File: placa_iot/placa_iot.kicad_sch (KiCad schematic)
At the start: 0 parts

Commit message: Esquemáticos creados
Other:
- added sheet ALIMENTACIÓN (alimentacion.kicad_sch)
- added sheet BATTERY (battery.kicad_sch)
- added sheet MICROCONTROLADOR (microcontrolador.kicad_sch)
- added sheet RF (rf.kicad_sch)
- company: (none) -> ELE0226
- title: (none) -> Placa IoT
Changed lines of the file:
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@@
 	(generator "eeschema")
 	(generator_version "10.0")
-	(paper "A4")
+	(paper "A3")
+	(title_block
+		(title "Placa IoT")
+		(date "2026-05-19")
+		(rev "R0")
+		(company "ELE0226")
+		(comment 1 "Sofía González Carranza")
+	)
+	(sheet
+		(at 40.64 151.13)
+		(size 105.41 92.71)
+		(exclude_from_sim no)
+		(in_bom yes)
+		(on_board yes)
+		(dnp no)
+		(fields_autoplaced yes)
+		(stroke
+			(width 0.1524)
+			(type solid)
+		)
+		(fill
+			(color 0 0 0 0)
+		)
+		(property "Sheetname" "RF"
+			(at 40.64 150.4184 0)
+			(show_name no)
+			(do_not_autoplace no)
+			(effects
+				(font
+					(size 1.27 1.27)
+				)
+				(justify left bottom)
+			)
+		)
+		(property "Sheetfile" "rf.kicad_sch"
+			(at 40.64 244.4246 0)
+			(show_name no)
+			(do_not_autoplace no)
+			(effects
+				(font
+					(size 1.27 1.27)
+				)
+				(justify left top)
+			)
+		)
+		(instances
+			(project "placa_iot"
+				(path "/ca8a6ff9-ef79-4432-921e-b6a14ecba63b"
+					(page "4")
+				)
+			)
+		)
+	)
+	(sheet
+		(at 38.1 38.1)
+		(size 107.95 90.17)
+		(exclude_from_sim no)
+		(in_bom yes)
+		(on_board yes)
+		(dnp no)
+		(fields_autoplaced yes)
+		(stroke
+			(width 0.1524)
+			(type solid)
+		)
+		(fill
+			(color 0 0 0 0)
+		)
+		(property "Sheetname" "ALIMENTACIÓN"
+			(at 38.1 37.3884 0)
+			(show_name no)
+			(do_not_autoplace no)
+			(effects
+				(font
+					(size 1.27 1.27)
+				)
+				(justify left bottom)
+			)
+		)
+		(property "Sheetfile" "alimentacion.kicad_sch"
+			(at 38.1 128.8546 0)
+			(show_name no)
+			(do_not_autoplace no)
+			(effects
+				(font
+					(size 1.27 1.27)
+				)
+				(justify left top)
+			)
+		)
+		(instances
+			(project "placa_iot"
+				(path "/ca8a6ff9-ef79-4432-921e-b6a14ecba63b"
+					(page "2")
+				)
+			)
+		)
+	)
+	(sheet
+		(at 294.64 85.09)
+		(size 99.06 109.22)
+		(exclude_from_sim no)
+		(in_bom yes)
+		(on_board yes)
+		(dnp no)
+		(fields_autoplaced yes)
+		(stroke
+			(width 0.1524)
+			(type solid)
+		)
+		(fill
+			(color 0 0 0 0)
+		)
+		(property "Sheetname" "BATTERY"
+			(at 294.64 84.3784 0)
+			(show_name no)
+			(do_not_autoplace no)
+			(effects
+				(font
+					(size 1.27 1.27)
+				)
+				(justify left bottom)
+			)
+		)
+		(property "Sheetfile" "battery.kicad_sch"
+			(at 294.64 194.8946 0)
+			(show_name no)
+			(do_not_autoplace no)
+			(effects
+				(font
+					(size 1.27 1.27)
+				)
+				(justify left top)
+			)
+		)
+		(instances
+			(project "placa_iot"
+				(path "/ca8a6ff9-ef79-4432-921e-b6a14ecba63b"
+					(page "5")
+				)
+			)
+		)
+	)
+	(sheet
+		(at 170.18 38.1)
+		(size 105.41 205.74)
+		(exclude_from_sim no)
+		(in_bom yes)
+		(on_board yes)
+		(dnp no)
+		(fields_autoplaced yes)
+		(stroke
+			(width 0.1524)
+			(type solid)
+		)
+		(fill
+			(color 0 0 0 0)
+		)
+		(property "Sheetname" "MICROCONTROLADOR"
+			(at 170.18 37.3884 0)
+			(show_name no)
+			(do_not_autoplace no)
+			(effects
+				(font
+					(size 1.27 1.27)
+				)
+				(justify left bottom)
+			)
+		)
+		(property "Sheetfile" "microcontrolador.kicad_sch"
+			(at 170.18 244.4246 0)
+			(show_name no)
+			(do_not_autoplace no)
+			(effects
+				(font
+					(size 1.27 1.27)
+				)
+				(justify left top)
+			)
+		)
+		(instances
+			(project "placa_iot"
+				(path "/ca8a6ff9-ef79-4432-921e-b6a14ecba63b"
+					(page "3")
+				)
+			)
+		)
+	)
 	(sheet_instances
 		(path "/"

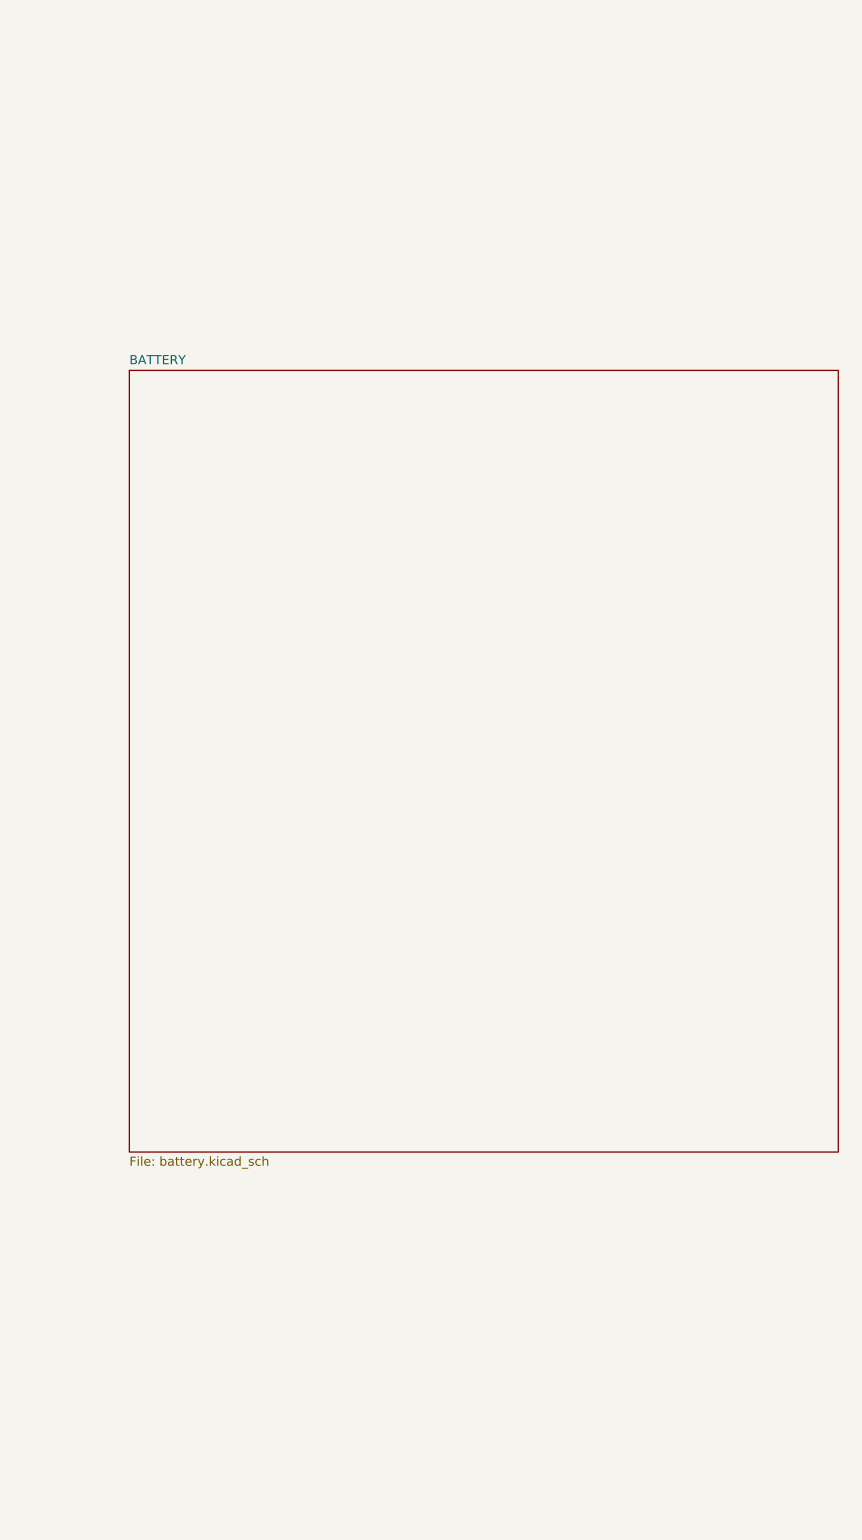
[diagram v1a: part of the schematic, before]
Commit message: Esquemático USB completado
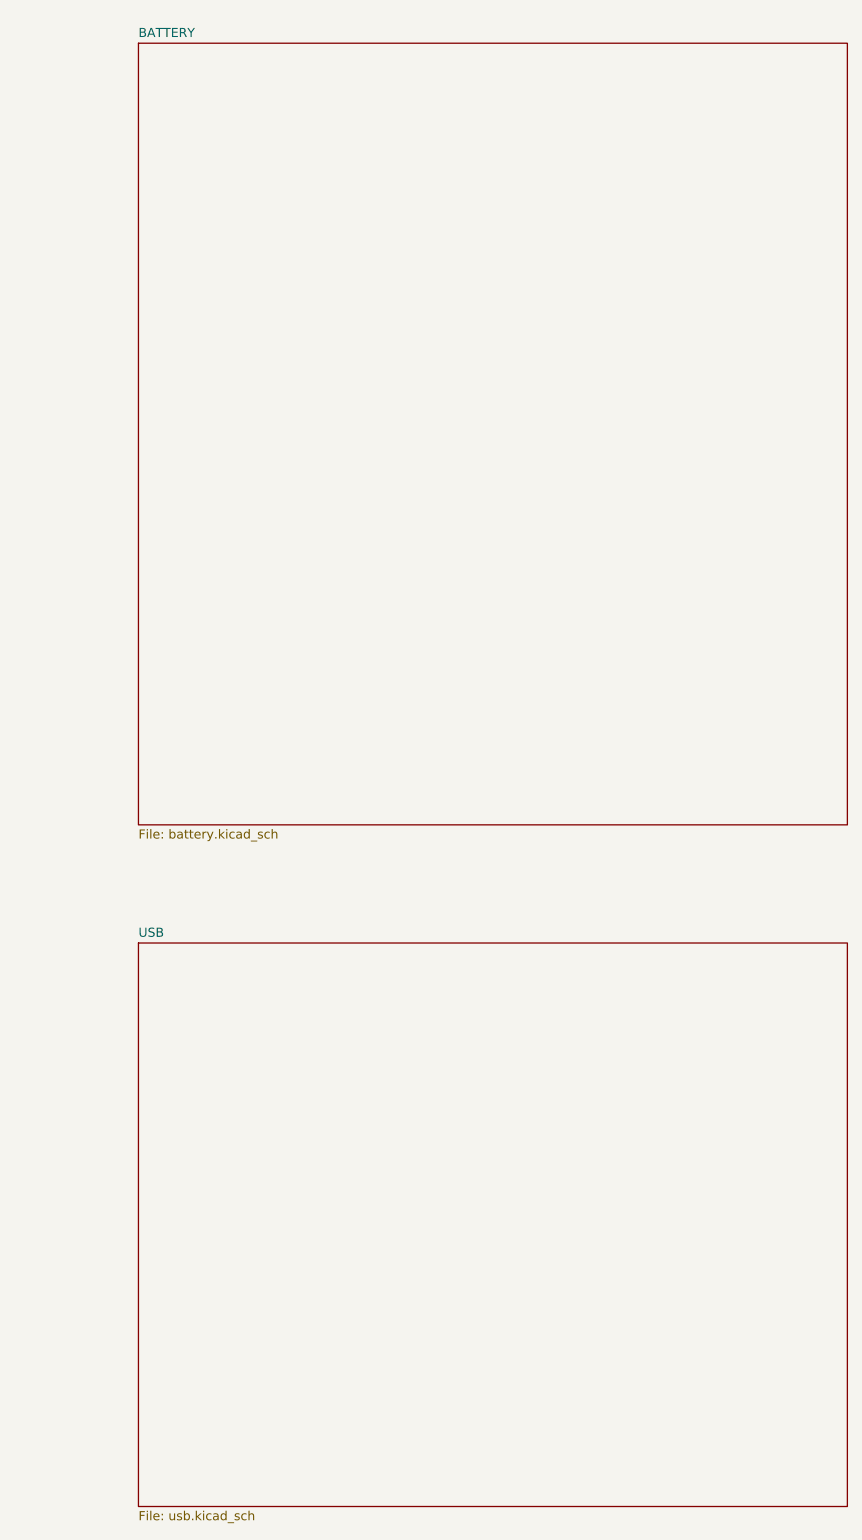
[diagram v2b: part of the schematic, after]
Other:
- added sheet USB (usb.kicad_sch)
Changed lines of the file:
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@@
 	)
 	(sheet
-		(at 294.64 85.09)
+		(at 295.91 39.37)
 		(size 99.06 109.22)
 		(exclude_from_sim no)
@@
 		)
 		(property "Sheetname" "BATTERY"
-			(at 294.64 84.3784 0)
+			(at 295.91 38.6584 0)
 			(show_name no)
 			(do_not_autoplace no)
@@
 		)
 		(property "Sheetfile" "battery.kicad_sch"
-			(at 294.64 194.8946 0)
+			(at 295.91 149.1746 0)
 			(show_name no)
 			(do_not_autoplace no)
@@
 				)
 			)
+		)
+	)
+	(sheet
+		(at 295.91 165.1)
+		(size 99.06 78.74)
+		(exclude_from_sim no)
+		(in_bom yes)
+		(on_board yes)
+		(dnp no)
+		(fields_autoplaced yes)
+		(stroke
+			(width 0.1524)
+			(type solid)
+		)
+		(fill
+			(color 0 0 0 0)
+		)
+		(property "Sheetname" "USB"
+			(at 295.91 164.3884 0)
+			(show_name no)
+			(do_not_autoplace no)
+			(effects
+				(font
+					(size 1.27 1.27)
+				)
+				(justify left bottom)
+			)
+		)
+		(property "Sheetfile" "usb.kicad_sch"
+			(at 295.91 244.4246 0)
+			(show_name no)
+			(do_not_autoplace no)
+			(effects
+				(font
+					(size 1.27 1.27)
+				)
+				(justify left top)
+			)
+		)
+		(instances
+			(project "placa_iot"
+				(path "/ca8a6ff9-ef79-4432-921e-b6a14ecba63b"
+					(page "6")
+				)
+			)

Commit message: Esquemático acabado
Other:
- sheet ALIMENTACIÓN ports: added IO35; removed none
- sheet BATTERY ports: added IO1, IO4; removed none
- sheet MICROCONTROLADOR ports: added D+, D-, IO1, IO3, IO33, IO34, IO35, IO36, IO4, IO5, IO6, IO7, IO8, IO9, LORA_RX, LORA_TX; removed none
- sheet RF ports: added IO3, IO33, IO34, IO36, IO5, IO6, IO7, IO8, IO9, LORA_RX, LORA_TX; removed none
- sheet USB ports: added D+, D-; removed none
